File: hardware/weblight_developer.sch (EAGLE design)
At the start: 14 parts, among them U1 ATtiny85-20SU

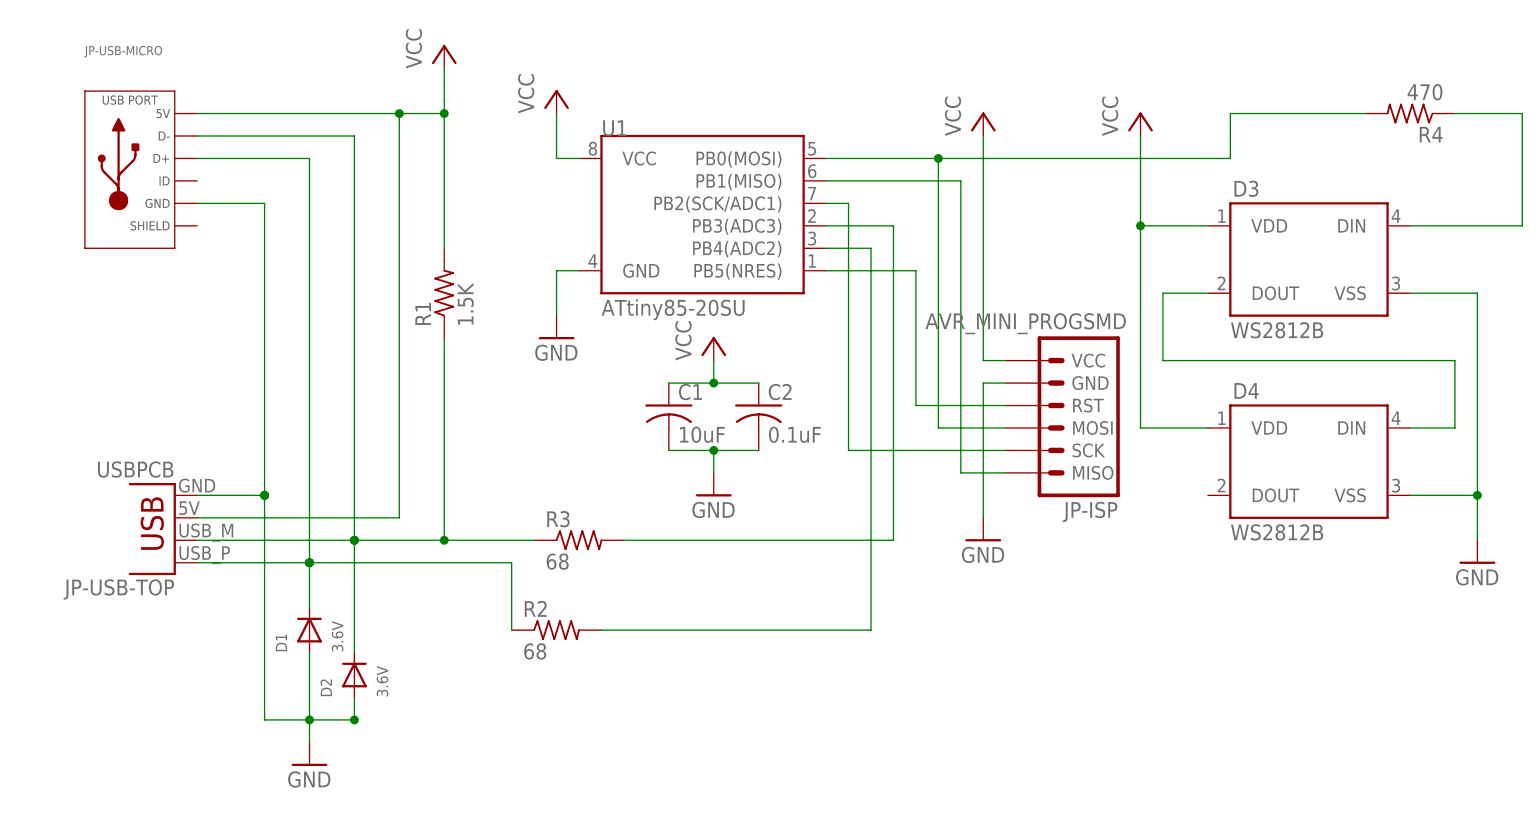
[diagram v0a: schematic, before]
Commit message: Developer board changes.
Convert every 0402 SMD to 0805.
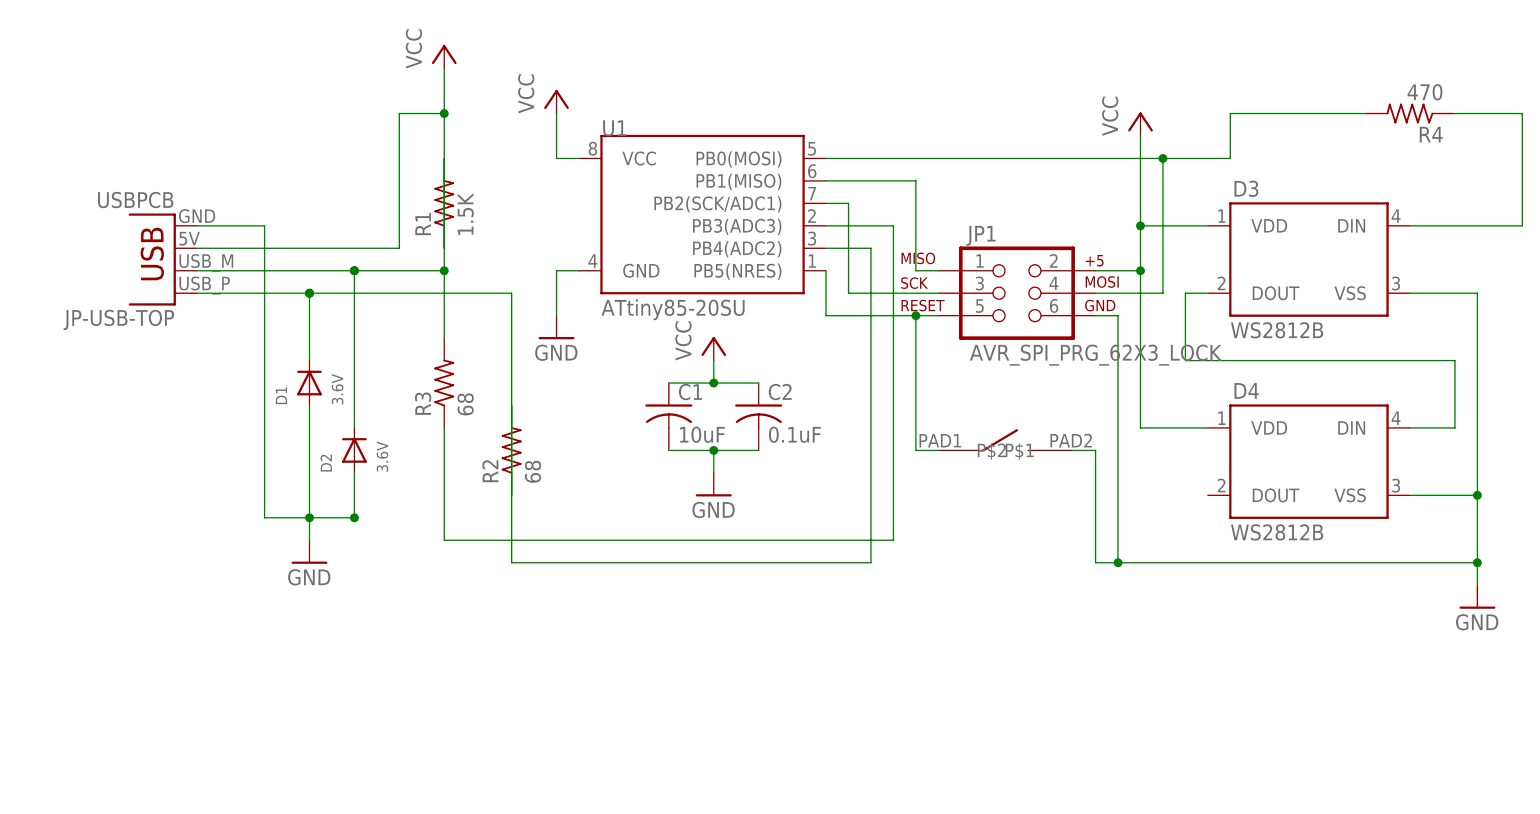
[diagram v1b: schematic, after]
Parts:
- removed JP-ISP: AVR_MINI_PROGSMD, SparkFun-Connectors:AVR_MINI_PROGSMD
- removed JP-USB-MICRO: (no value), MF_Connectors:USB_MICRO_RIGHT
- added JP1: AVR_SPI_PRG_62X3_LOCK, SparkFun-Connectors:AVR_SPI_PRG_62X3_LOCK
- added SW_RESET: BUTTON_TD-85XU, weblight:BUTTON_TD-85XU
- C1, C2: device rcl:C-USC0402 -> rcl:C-USC0805
- D1, D2: device microbuilder:DIODESOD-523 -> microbuilder:DIODESOD-323
- R1, R2, R3, R4: device rcl:R-US_R0402 -> rcl:R-US_R0805
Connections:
- net N$1 renamed DIN_1
- removed net MOSI/DIN: JP-ISP.MOSI, R4.2, U1.PB0(MOSI)
- new net MOSI/DIN_RAW: JP1.4, R4.2, U1.PB0(MOSI)
- net GND: now also JP1.6, SW_RESET.P$2; no longer JP-ISP.GND, JP-USB-MICRO.GND
- net MISO: now also JP1.1; no longer JP-ISP.MISO
- net RESET: now also JP1.5, SW_RESET.P$1; no longer JP-ISP.RST
- net SCK: now also JP1.3; no longer JP-ISP.SCK
- net USB_D_MINUS: now also R3.1; no longer R3.2
- net USB_D_MINUS_RAW: now also R1.2, R3.2; no longer JP-USB-MICRO.D-, R1.1, R3.1
- net USB_D_PLUS_RAW: no longer JP-USB-MICRO.D+
- net VCC: now also JP1.2, R1.1; no longer JP-ISP.VCC, JP-USB-MICRO.5V, R1.2
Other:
- moved on the sheet: D1, D2, JP-USB-TOP, R1, R2, R3

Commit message: osh3 rc1
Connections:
- net USB_D_MINUS_RAW: now also R1.1; no longer R1.2
- net USB_D_PLUS: now also R2.1; no longer R2.2
- net USB_D_PLUS_RAW: now also R2.2; no longer R2.1
- net VCC: now also R1.2; no longer R1.1
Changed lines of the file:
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@@
 <grid distance="0.1" unitdist="inch" unit="inch" style="lines" multiple="1" display="no" altdistance="0.01" altunitdist="inch" altunit="inch"/>
 <layers>
-<layer number="1" name="Top" color="4" fill="1" visible="yes" active="no"/>
-<layer number="16" name="Bottom" color="1" fill="1" visible="yes" active="no"/>
-<layer number="17" name="Pads" color="2" fill="1" visible="yes" active="no"/>
-<layer number="18" name="Vias" color="2" fill="1" visible="yes" active="no"/>
-<layer number="19" name="Unrouted" color="6" fill="1" visible="yes" active="no"/>
-<layer number="20" name="Dimension" color="15" fill="1" visible="yes" active="no"/>
-<layer number="21" name="tPlace" color="7" fill="1" visible="yes" active="no"/>
-<layer number="22" name="bPlace" color="7" fill="1" visible="yes" active="no"/>
-<layer number="23" name="tOrigins" color="15" fill="1" visible="yes" active="no"/>
-<layer number="24" name="bOrigins" color="15" fill="1" visible="yes" active="no"/>
-<layer number="25" name="tNames" color="7" fill="1" visible="yes" active="no"/>
-<layer number="26" name="bNames" color="7" fill="1" visible="yes" active="no"/>
-<layer number="27" name="tValues" color="7" fill="1" visible="yes" active="no"/>
-<layer number="28" name="bValues" color="7" fill="1" visible="yes" active="no"/>
+<layer number="1" name="Top" color="4" fill="1" visible="no" active="no"/>
+<layer number="16" name="Bottom" color="1" fill="1" visible="no" active="no"/>
+<layer number="17" name="Pads" color="2" fill="1" visible="no" active="no"/>
+<layer number="18" name="Vias" color="2" fill="1" visible="no" active="no"/>
+<layer number="19" name="Unrouted" color="6" fill="1" visible="no" active="no"/>
+<layer number="20" name="Dimension" color="15" fill="1" visible="no" active="no"/>
+<layer number="21" name="tPlace" color="7" fill="1" visible="no" active="no"/>
+<layer number="22" name="bPlace" color="7" fill="1" visible="no" active="no"/>
+<layer number="23" name="tOrigins" color="15" fill="1" visible="no" active="no"/>
+<layer number="24" name="bOrigins" color="15" fill="1" visible="no" active="no"/>
+<layer number="25" name="tNames" color="7" fill="1" visible="no" active="no"/>
+<layer number="26" name="bNames" color="7" fill="1" visible="no" active="no"/>
+<layer number="27" name="tValues" color="7" fill="1" visible="no" active="no"/>
+<layer number="28" name="bValues" color="7" fill="1" visible="no" active="no"/>
 <layer number="29" name="tStop" color="7" fill="3" visible="no" active="no"/>
 <layer number="30" name="bStop" color="7" fill="6" visible="no" active="no"/>
@@
 <layer number="35" name="tGlue" color="7" fill="4" visible="no" active="no"/>
 <layer number="36" name="bGlue" color="7" fill="5" visible="no" active="no"/>
-<layer number="37" name="tTest" color="7" fill="1" visible="yes" active="no"/>
-<layer number="38" name="bTest" color="7" fill="1" visible="yes" active="no"/>
+<layer number="37" name="tTest" color="7" fill="1" visible="no" active="no"/>
+<layer number="38" name="bTest" color="7" fill="1" visible="no" active="no"/>
 <layer number="39" name="tKeepout" color="4" fill="11" visible="no" active="no"/>
 <layer number="40" name="bKeepout" color="1" fill="11" visible="no" active="no"/>
@@
 <layer number="44" name="Drills" color="7" fill="1" visible="no" active="no"/>
 <layer number="45" name="Holes" color="7" fill="1" visible="no" active="no"/>
-<layer number="46" name="Milling" color="3" fill="1" visible="yes" active="no"/>
-<layer number="47" name="Measures" color="7" fill="1" visible="yes" active="no"/>
-<layer number="48" name="Document" color="7" fill="1" visible="yes" active="no"/>
-<layer number="49" name="Reference" color="7" fill="1" visible="yes" active="no"/>
-<layer number="50" name="dxf" color="7" fill="1" visible="yes" active="no"/>
-<layer number="51" name="tDocu" color="7" fill="1" visible="yes" active="no"/>
-<layer number="52" name="bDocu" color="7" fill="1" visible="yes" active="no"/>
-<layer number="53" name="tGND_GNDA" color="7" fill="9" visible="yes" active="no"/>
-<layer number="54" name="bGND_GNDA" color="1" fill="9" visible="yes" active="no"/>
-<layer number="56" name="wert" color="7" fill="1" visible="yes" active="no"/>
-<layer number="57" name="tCAD" color="7" fill="1" visible="yes" active="no"/>
-<layer number="59" name="tCarbon" color="7" fill="1" visible="yes" active="no"/>
-<layer number="60" name="bCarbon" color="7" fill="1" visible="yes" active="no"/>
+<layer number="46" name="Milling" color="3" fill="1" visible="no" active="no"/>
+<layer number="47" name="Measures" color="7" fill="1" visible="no" active="no"/>
+<layer number="48" name="Document" color="7" fill="1" visible="no" active="no"/>
+<layer number="49" name="Reference" color="7" fill="1" visible="no" active="no"/>
+<layer number="50" name="dxf" color="7" fill="1" visible="no" active="no"/>
+<layer number="51" name="tDocu" color="7" fill="1" visible="no" active="no"/>
+<layer number="52" name="bDocu" color="7" fill="1" visible="no" active="no"/>
+<layer number="53" name="tGND_GNDA" color="7" fill="9" visible="no" active="no"/>
+<layer number="54" name="bGND_GNDA" color="1" fill="9" visible="no" active="no"/>
+<layer number="56" name="wert" color="7" fill="1" visible="no" active="no"/>
+<layer number="57" name="tCAD" color="7" fill="1" visible="no" active="no"/>
+<layer number="59" name="tCarbon" color="7" fill="1" visible="no" active="no"/>
+<layer number="60" name="bCarbon" color="7" fill="1" visible="no" active="no"/>
 <layer number="90" name="Modules" color="5" fill="1" visible="yes" active="yes"/>
 <layer number="91" name="Nets" color="2" fill="1" visible="yes" active="yes"/>
@@
 <pinref part="JP-USB-TOP" gate="G$1" pin="VBUS"/>
 <wire x1="-45.72" y1="71.12" x2="-22.86" y2="71.12" width="0.1524" layer="91"/>
-<pinref part="R1" gate="G$1" pin="1"/>
+<pinref part="R1" gate="G$1" pin="2"/>
 <wire x1="-17.78" y1="86.36" x2="-22.86" y2="86.36" width="0.1524" layer="91"/>
 <junction x="-17.78" y="86.36"/>
 <pinref part="P+2" gate="VCC" pin="VCC"/>
 <wire x1="-17.78" y1="86.36" x2="-17.78" y2="91.44" width="0.1524" layer="91"/>
-<wire x1="-17.78" y1="71.12" x2="-17.78" y2="86.36" width="0.1524" layer="91"/>
+<wire x1="-17.78" y1="81.28" x2="-17.78" y2="86.36" width="0.1524" layer="91"/>
 <wire x1="-22.86" y1="71.12" x2="-22.86" y2="86.36" width="0.1524" layer="91"/>
 </segment>
@@
 <wire x1="-17.78" y1="60.96" x2="-17.78" y2="68.58" width="0.1524" layer="91"/>
 <pinref part="JP-USB-TOP" gate="G$1" pin="D-"/>
-<pinref part="R1" gate="G$1" pin="2"/>
+<pinref part="R1" gate="G$1" pin="1"/>
 <wire x1="-17.78" y1="68.58" x2="-27.94" y2="68.58" width="0.1524" layer="91"/>
 <wire x1="-27.94" y1="68.58" x2="-45.72" y2="68.58" width="0.1524" layer="91"/>
-<wire x1="-17.78" y1="81.28" x2="-17.78" y2="68.58" width="0.1524" layer="91"/>
+<wire x1="-17.78" y1="71.12" x2="-17.78" y2="68.58" width="0.1524" layer="91"/>
 <junction x="-17.78" y="68.58"/>
 <pinref part="D2" gate="G$1" pin="C"/>
@@
 <wire x1="-45.72" y1="66.04" x2="-33.02" y2="66.04" width="0.1524" layer="91"/>
 <wire x1="-33.02" y1="66.04" x2="-10.16" y2="66.04" width="0.1524" layer="91"/>
-<pinref part="R2" gate="G$1" pin="1"/>
-<wire x1="-10.16" y1="66.04" x2="-10.16" y2="43.18" width="0.1524" layer="91"/>
+<pinref part="R2" gate="G$1" pin="2"/>
+<wire x1="-10.16" y1="66.04" x2="-10.16" y2="53.34" width="0.1524" layer="91"/>
 <pinref part="D1" gate="G$1" pin="C"/>
 <wire x1="-33.02" y1="58.42" x2="-33.02" y2="66.04" width="0.1524" layer="91"/>
@@
 <net name="USB_D_PLUS" class="0">
 <segment>
-<pinref part="R2" gate="G$1" pin="2"/>
-<wire x1="-10.16" y1="53.34" x2="-10.16" y2="35.56" width="0.1524" layer="91"/>
+<pinref part="R2" gate="G$1" pin="1"/>
+<wire x1="-10.16" y1="43.18" x2="-10.16" y2="35.56" width="0.1524" layer="91"/>
 <wire x1="-10.16" y1="35.56" x2="30.48" y2="35.56" width="0.1524" layer="91"/>
 <wire x1="30.48" y1="35.56" x2="30.48" y2="71.12" width="0.1524" layer="91"/>

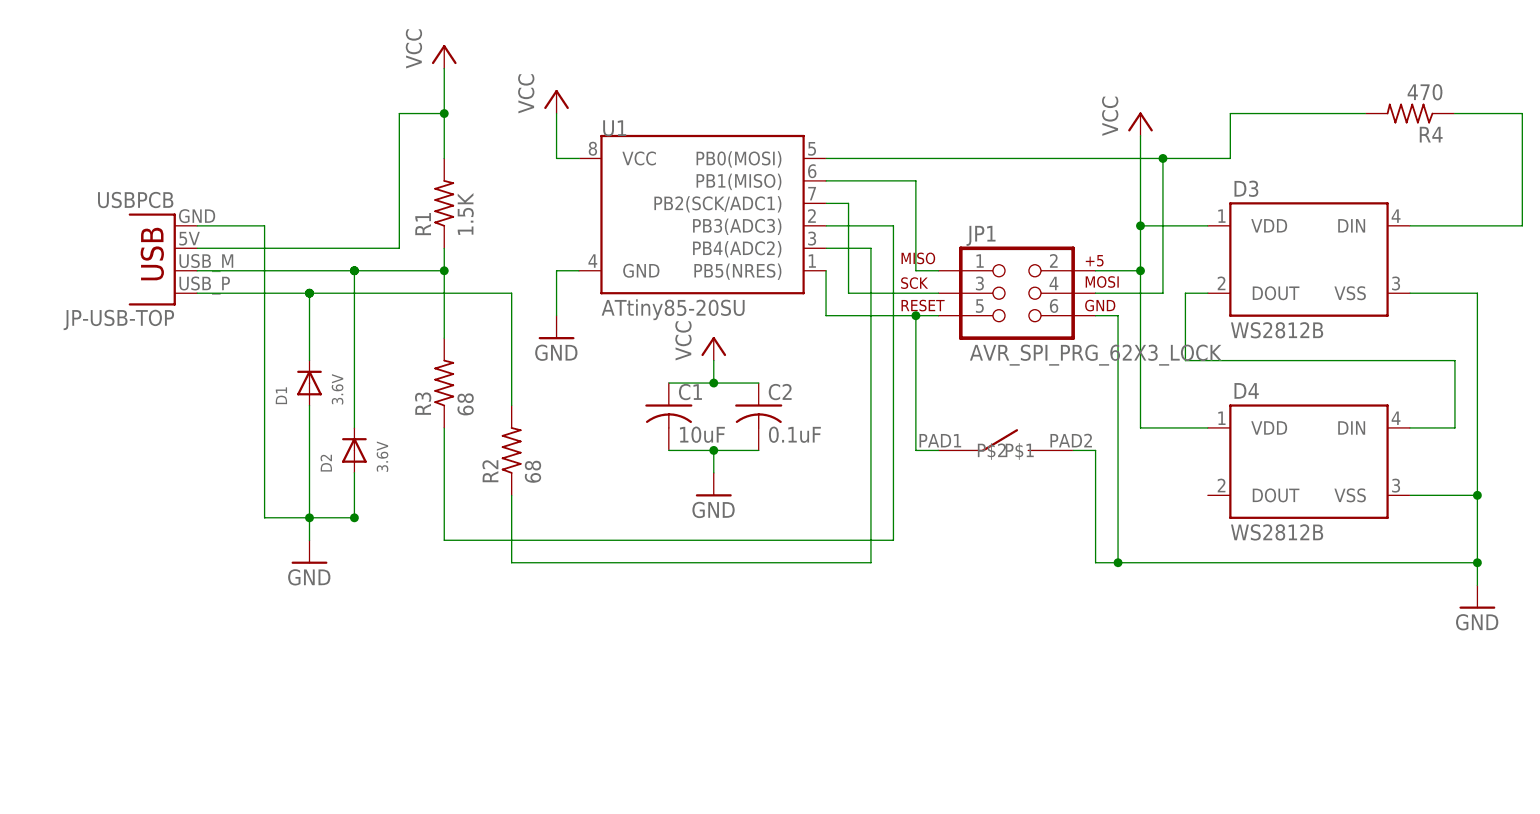
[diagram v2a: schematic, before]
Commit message: Move developer board to APA102C
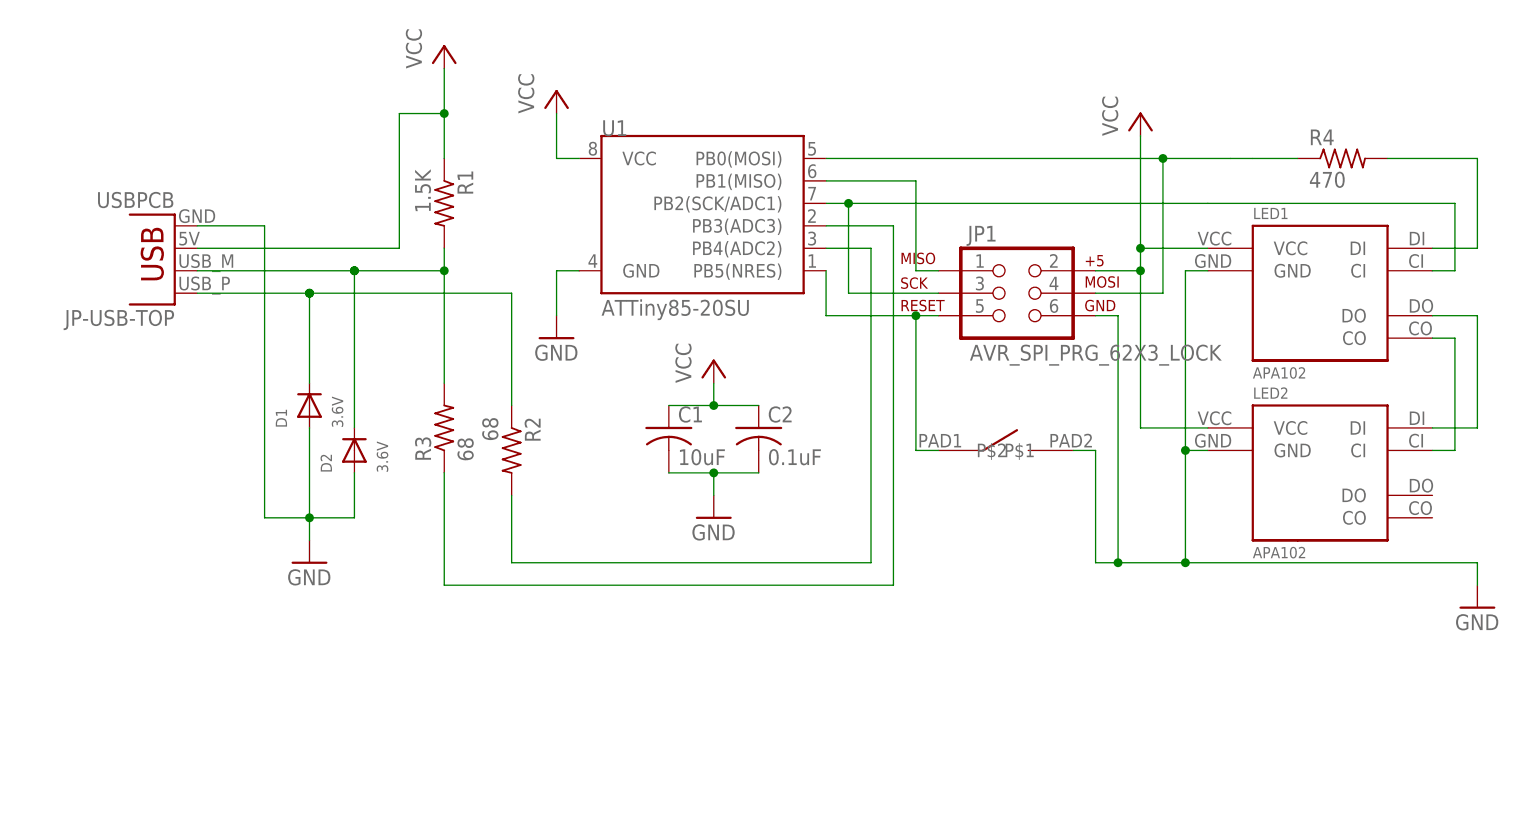
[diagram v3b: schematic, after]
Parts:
- removed D3, D4: WS2812B, SparkFun-LED:WS2812B
- added LED1, LED2: APA102, weblight:APA102
- U1: value ATtiny85-20SU -> ATTiny85-20SU
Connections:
- removed net SCK: JP1.3, U1.PB2(SCK/ADC1)
- new net SCK_1: JP1.3, LED1.CI, U1.PB2(SCK/ADC1)
- new net SCK_2: LED1.CO, LED2.CI
- net DIN_1: now also LED1.DI, R4.2; no longer D3.DIN, R4.1
- net DIN_2: now also LED1.DO, LED2.DI; no longer D3.DOUT, D4.DIN
- net GND: now also LED1.GND, LED2.GND; no longer D3.VSS, D4.VSS
- net MOSI/DIN_RAW: now also R4.1; no longer R4.2
- net USB_D_MINUS_RAW: now also R1.2; no longer R1.1
- net USB_D_PLUS: now also R2.2; no longer R2.1
- net USB_D_PLUS_RAW: now also R2.1; no longer R2.2
- net VCC: now also LED1.VCC, LED2.VCC, R1.1; no longer D3.VDD, D4.VDD, R1.2
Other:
- moved on the sheet: C1, C2, D1, R1, R2, R3, R4
